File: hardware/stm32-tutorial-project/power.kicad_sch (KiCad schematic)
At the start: 18 parts, among them J1 USB_C_Receptacle_USB2.0_14P, U2 AZ1117-3.3

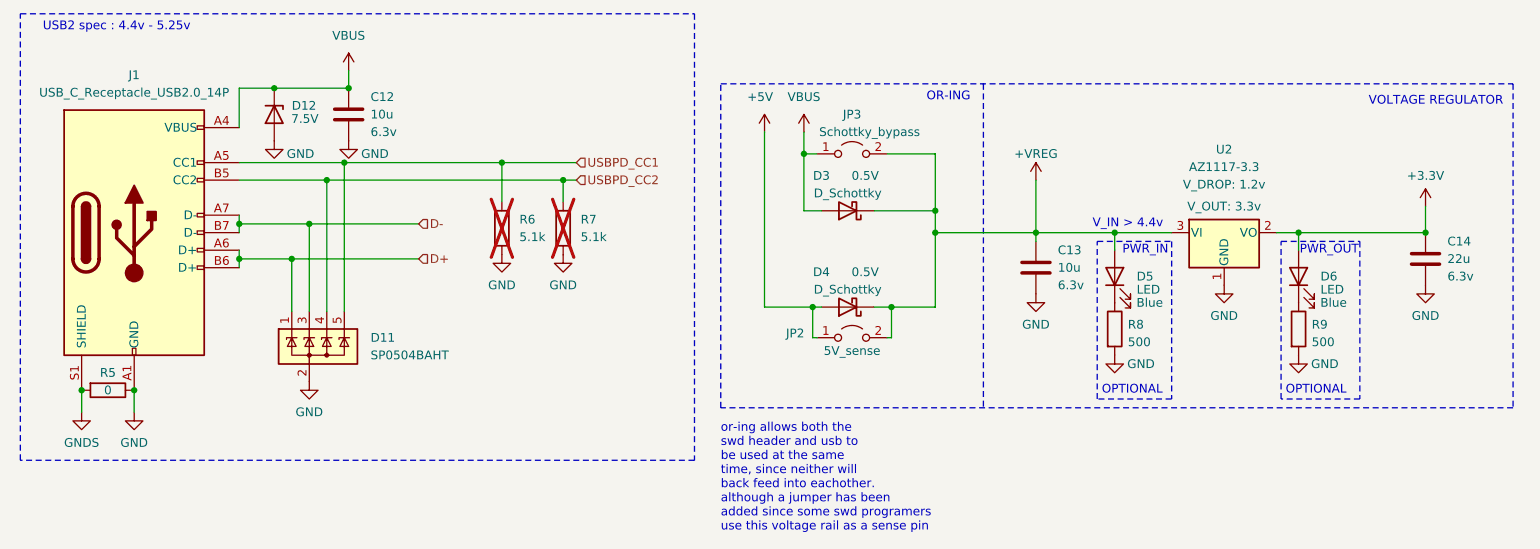
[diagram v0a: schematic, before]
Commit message: added fuse to power input
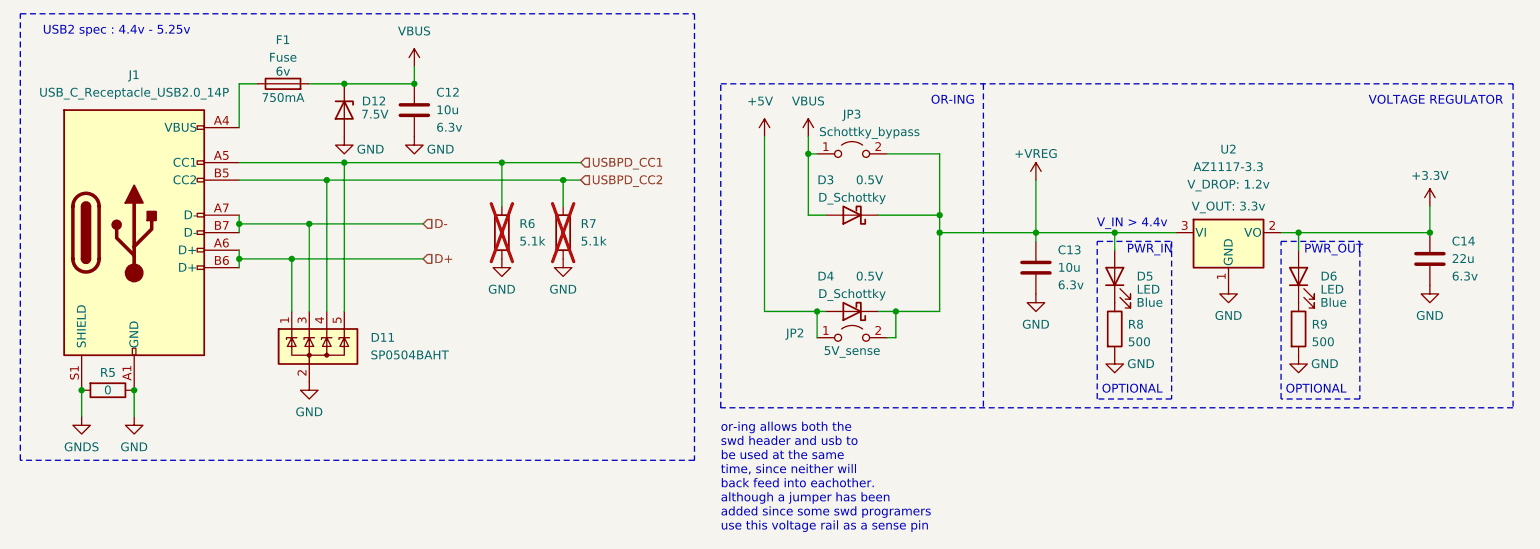
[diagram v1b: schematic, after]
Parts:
- added F1: Fuse, Fuse:Fuse_0805_2012Metric, symbol Device:Fuse
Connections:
- net VBUS: now also F1.2; no longer J1.A4 (VBUS), J1.A9 (VBUS), J1.B4 (VBUS), J1.B9 (VBUS)
- new net: F1.1, J1.A4 (VBUS), J1.A9 (VBUS), J1.B4 (VBUS), J1.B9 (VBUS)
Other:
- moved on the sheet: C12, C14, D12, D3, D4, R6, R7, U2

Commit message: added testpoints
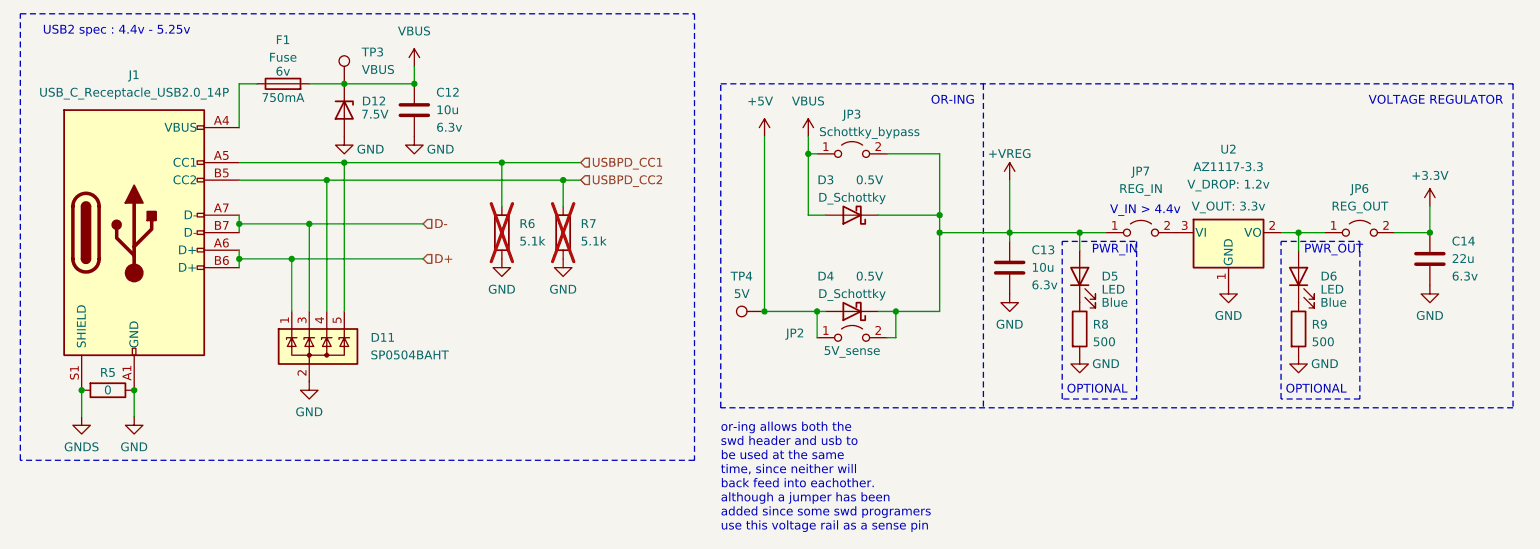
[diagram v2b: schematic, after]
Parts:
- added JP6: REG_OUT, symbol Jumper:Jumper_2_Open
- added JP7: REG_IN, symbol Jumper:Jumper_2_Open
- added TP3: VBUS, symbol Connector:TestPoint
- added TP4: 5V, symbol Connector:TestPoint
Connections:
- net +3.3V: now also JP6.2 (B); no longer D6.2 (A), U2.2 (VO)
- net +5V: now also TP4.1
- net +VREG: now also JP7.1 (A); no longer U2.3 (VI)
- net VBUS: now also TP3.1
- new net: D6.2 (A), JP6.1 (A), U2.2 (VO)
- new net: JP7.2 (B), U2.3 (VI)
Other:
- moved on the sheet: C13

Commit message: added supplier links, part numbers and datasheets
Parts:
- C12, C13: footprint (none) -> Capacitor_SMD:C_0603_1608Metric_Pad1.08x0.95mm_HandSolder; Part Number (none) -> C0603C106M9PACTU; supplier_link (none) -> https://www.digikey.co.nz/en/products/detail/kemet/C0603C10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
- C14: footprint (none) -> Capacitor_SMD:C_0603_1608Metric_Pad1.08x0.95mm_HandSolder; Part Number (none) -> C0805C226M9PACTU; supplier_link (none) -> https://www.digikey.co.nz/en/products/detail/kemet/C0805C22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
- D11: value SP0504BAHT -> SP0504BAHTG; Part Number (none) -> SP0504BAHTG; supplier_link (none) -> https://www.digikey.co.nz/en/products/detail/littelfuse-inc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
- D12: Part Number (none) -> PTVS7V5Z1USKYL; Votlage 7.5V -> (none); supplier_link (none) -> https://www.digikey.co.nz/en/products/detail/nexperia-usa-i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; votlage (none) -> 7.5V
- D3, D4: footprint (none) -> Diode_SMD:D_0603_1608Metric_Pad1.05x0.95mm_HandSolder; Part Number (none) -> SD0805S020S1R0; supplier_link (none) -> https://www.digikey.co.nz/en/products/detail/kyocera-avx/SD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
- D5, D6: footprint (none) -> Diode_SMD:D_0603_1608Metric_Pad1.05x0.95mm_HandSolder; Part Number (none) -> 150060BS75000; supplier_link (none) -> https://www.digikey.co.nz/en/products/detail/w%C3%BCrth-ele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
- F1: Part Number (none) -> 0ZCK0075FF2E; supplier_link (none) -> https://www.digikey.co.nz/en/products/detail/bel-fuse-inc/0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
- J1: footprint (none) -> Connector_USB:USB_C_Receptacle_HRO_TYPE-C-31-M-12; Part Number (none) -> USB4105-GF-A; supplier_link (none) -> https://www.digikey.co.nz/en/products/detail/gct/USB4105-GF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
- JP2, JP3, JP6, JP7, TP3, TP4: now left out of the parts list
- R5: footprint (none) -> Resistor_SMD:R_0603_1608Metric_Pad0.98x0.95mm_HandSolder; Part Number (none) -> RC0603JR-070RL; supplier_link (none) -> https://www.digikey.co.nz/en/products/detail/yageo/RC0603JR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
- R6, R7: footprint (none) -> Resistor_SMD:R_0603_1608Metric_Pad0.98x0.95mm_HandSolder; Part Number (none) -> RC0603FR-075K1L; supplier_link (none) -> https://www.digikey.co.nz/en/products/detail/yageo/RC0603FR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
- R8, R9: footprint (none) -> Resistor_SMD:R_0603_1608Metric_Pad0.98x0.95mm_HandSolder; Part Number (none) -> RT0603BRD07500RL; supplier_link (none) -> https://www.digikey.co.nz/en/products/detail/yageo/RT0603BR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
- U2: footprint (none) -> Package_TO_SOT_SMD:SOT-223-3_TabPin2; Part Number (none) -> AZ1117CH-3.3TRG1; supplier_link (none) -> https://www.digikey.co.nz/en/products/detail/diodes-incorpo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

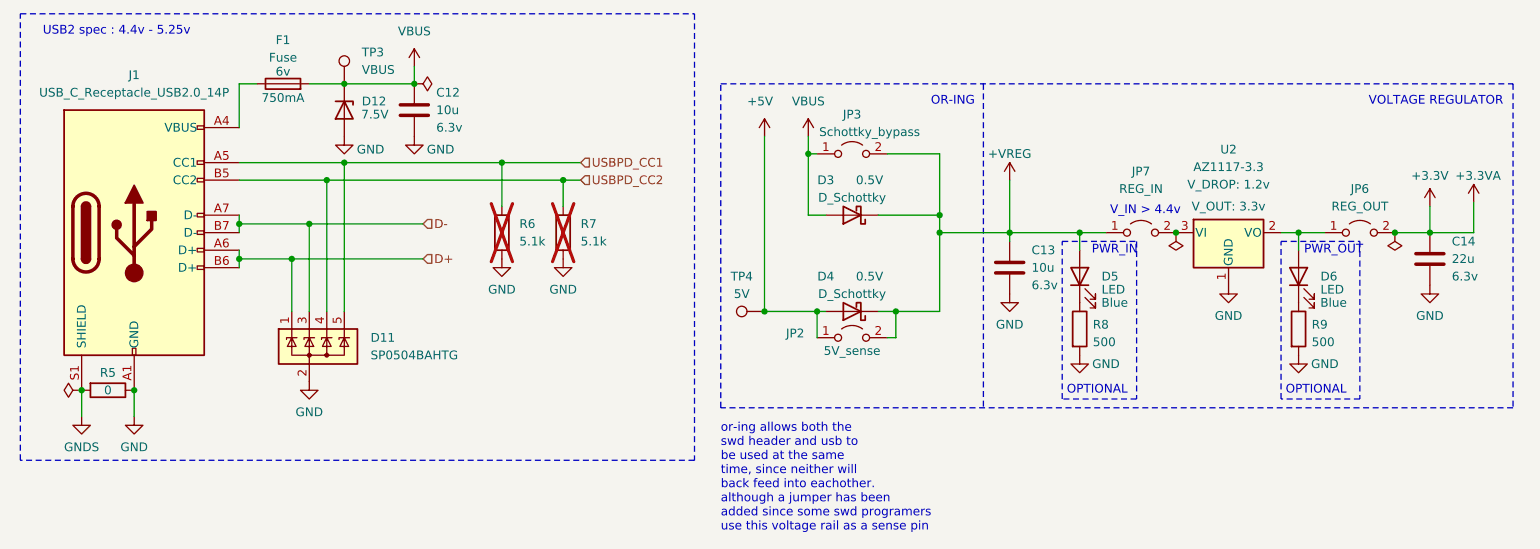
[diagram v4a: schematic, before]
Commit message: added footprints to the jumpers
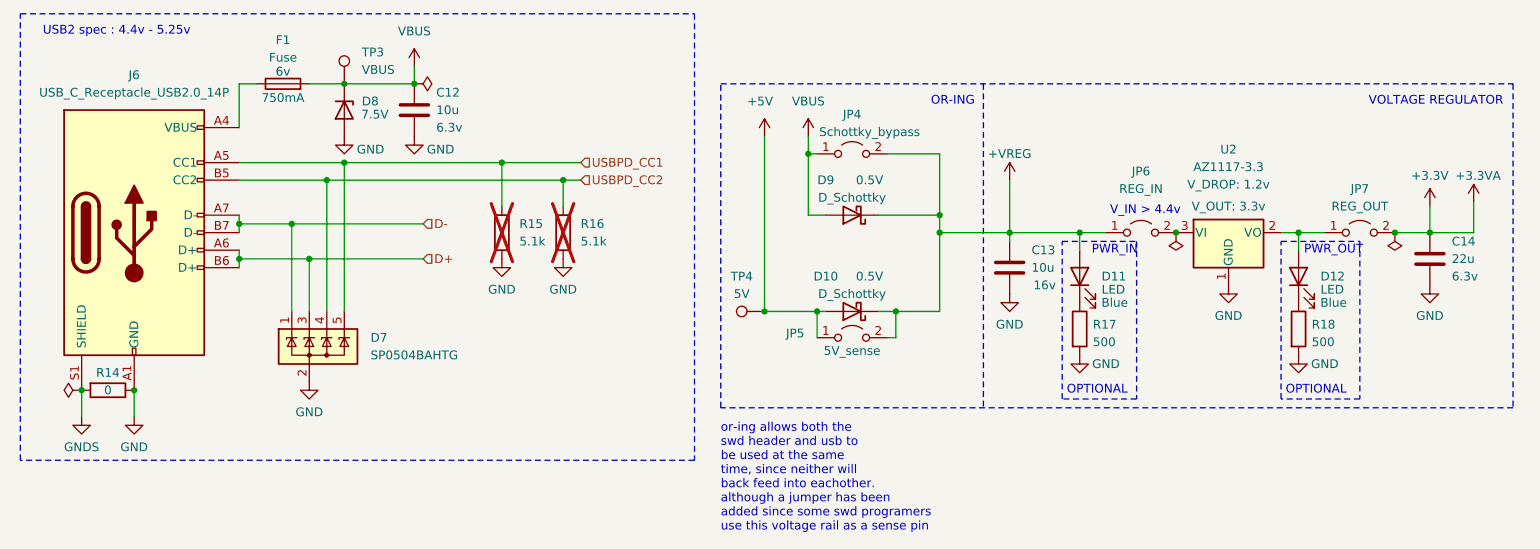
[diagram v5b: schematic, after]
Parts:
- C13: footprint Capacitor_SMD:C_0603_1608Metric_Pad1.08x0.95mm_HandSolder -> Capacitor_SMD:C_0805_2012Metric_Pad1.18x1.45mm_HandSolder; Part Number C0603C106M9PACTU -> C0805C106K4PACTU; supplier_link https://www.digikey.co.nz/en/products/detail/kemet/C0603C10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 -> https://www.digikey.co.nz/en/products/detail/kemet/C0805C10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; voltage 6.3v -> 16v
- JP4: renamed from JP3; footprint (none) -> Jumper:SolderJumper-2_P1.3mm_Open_Pad1.0x1.5mm
- JP5: renamed from JP2; footprint (none) -> Jumper:SolderJumper-2_P1.3mm_Open_Pad1.0x1.5mm
- JP6: renamed from JP7; footprint (none) -> Jumper:SolderJumper-2_P1.3mm_Open_Pad1.0x1.5mm
- JP7: renamed from JP6; footprint (none) -> Jumper:SolderJumper-2_P1.3mm_Open_Pad1.0x1.5mm
- TP3, TP4: footprint (none) -> TestPoint:TestPoint_Pad_3.0x3.0mm
- renumbered D4 to D10, D5 to D11, D6 to D12, D11 to D7, D12 to D8, D3 to D9, J1 to J6, R5 to R14, R6 to R15, R7 to R16, R8 to R17, R9 to R18
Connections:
- net D+: now also D7.3 (K); no longer D7.1 (K)
- net D-: now also D7.1 (K); no longer D7.3 (K)
